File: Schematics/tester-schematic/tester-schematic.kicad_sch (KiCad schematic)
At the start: 1 part

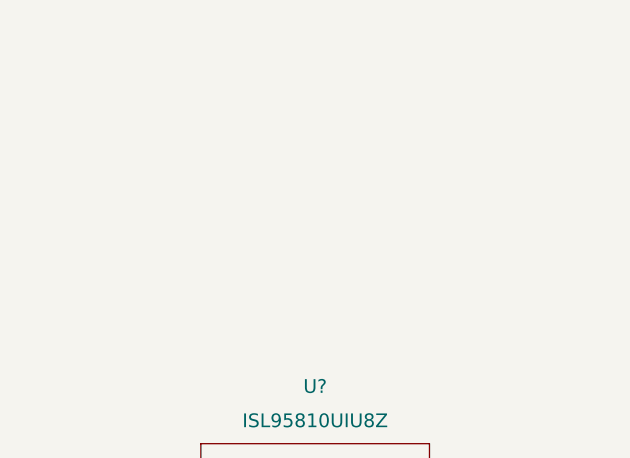
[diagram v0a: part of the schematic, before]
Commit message: added buck converter library
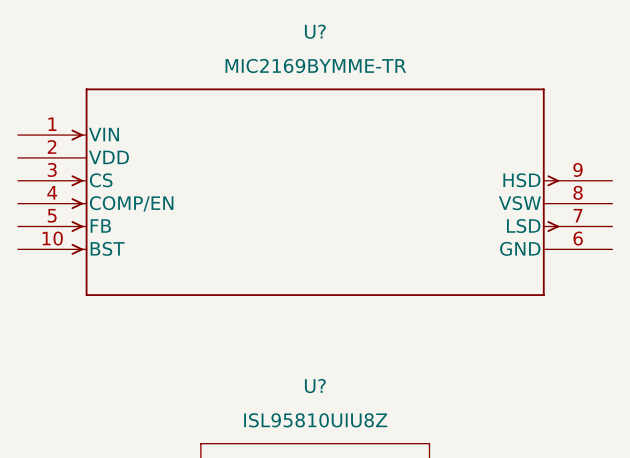
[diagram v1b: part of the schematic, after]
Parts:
- added U?: MIC2169BYMME-TR, MSOP-10_MM_MCH, symbol buck:MIC2169BYMME-TR
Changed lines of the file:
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@@
     (pin "8")
+  )
+  (symbol (lib_id "buck:MIC2169BYMME-TR") (at 104.14 52.07 0) (unit 1)
+    (in_bom yes) (on_board yes) (fields_autoplaced)
+    (property "Reference" "U?" (id 0) (at 137.16 40.64 0)
+      (effects (font (size 1.524 1.524)))
+    )
+    (property "Value" "MIC2169BYMME-TR" (id 1) (at 137.16 44.45 0)
+      (effects (font (size 1.524 1.524)))
+    )
+    (property "Footprint" "MSOP-10_MM_MCH" (id 2) (at 137.16 45.974 0)
+      (effects (font (size 1.524 1.524)) hide)
+    )
+    (property "Datasheet" "" (id 3) (at 104.14 52.07 0)
+      (effects (font (size 1.524 1.524)))
+    )
+    (pin "1")
+    (pin "10")
+    (pin "2")
+    (pin "3")
+    (pin "4")
+    (pin "5")
+    (pin "6")
+    (pin "7")
+    (pin "8")
+    (pin "9")
   )
   (sheet_instances
@@
       (reference "U?") (unit 1) (value "ISL95810UIU8Z") (footprint "MSOP8_3P05X3P05_INR")
     )
+    (path "/eba1abb3-bc61-46a2-bdc4-c956629aef7c"
+      (reference "U?") (unit 1) (value "MIC2169BYMME-TR") (footprint "MSOP-10_MM_MCH")
+    )
   )

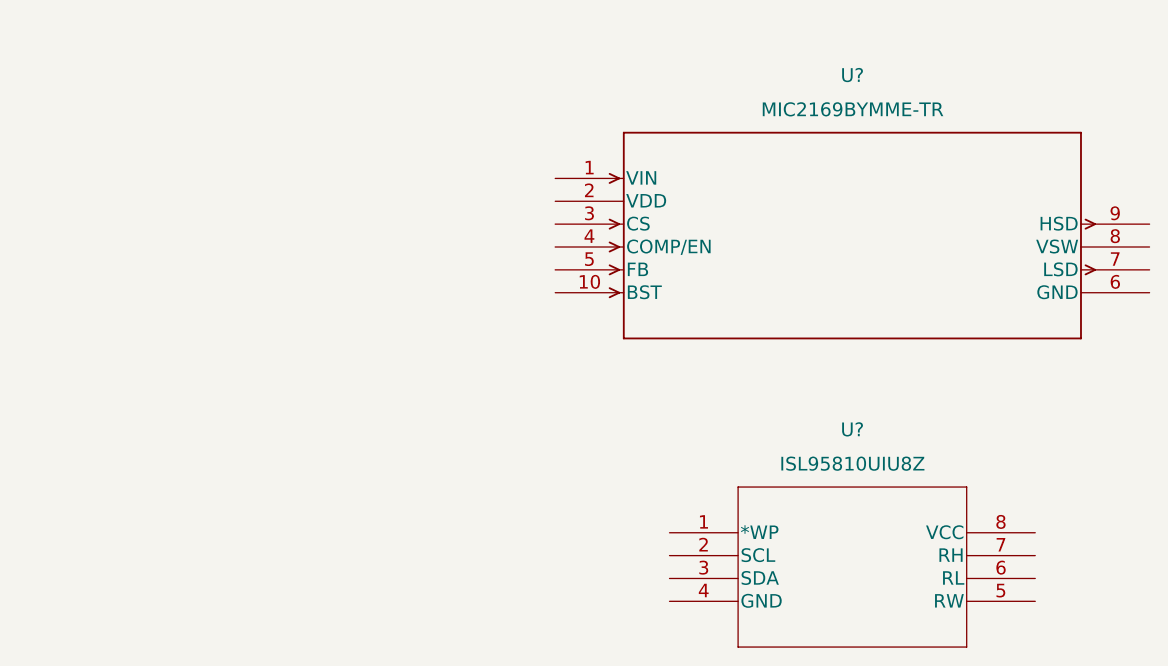
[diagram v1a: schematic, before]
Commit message: buck converter, dig pot, and surrounding components incomplete
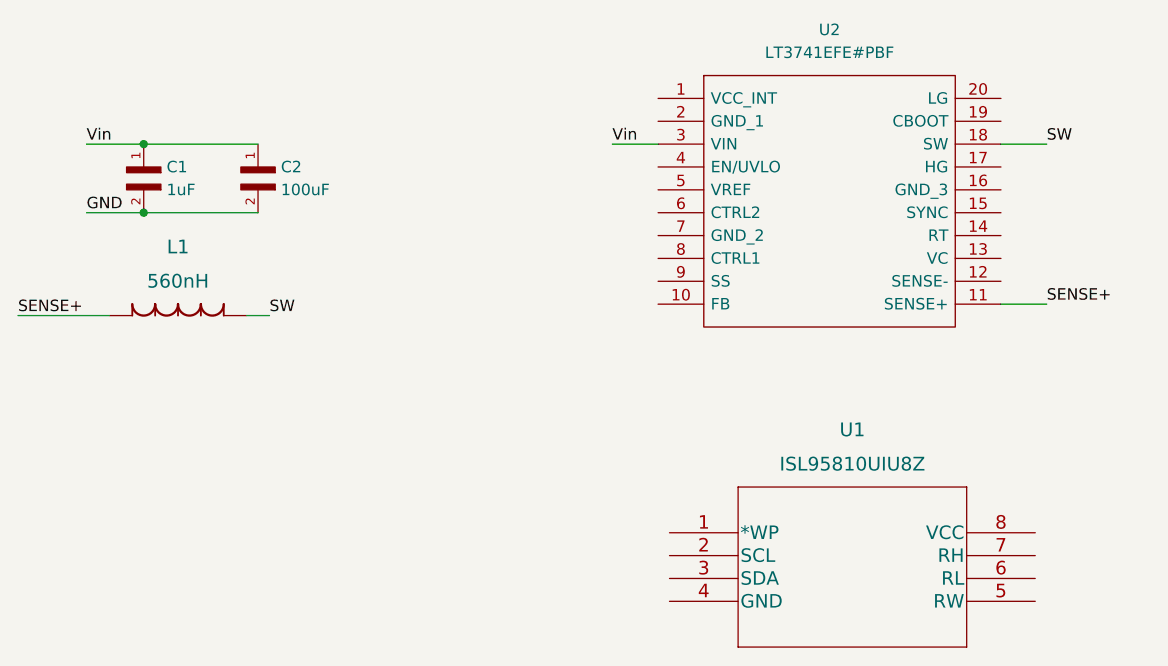
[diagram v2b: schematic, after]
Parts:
- removed U?: MIC2169BYMME-TR, MSOP-10_MM_MCH, symbol buck:MIC2169BYMME-TR
- added C1: 1uF, CAPC2012X127N, symbol 0805cap:S-0805
- added C2: 100uF, CAPC2012X127N, symbol 0805cap:S-0805
- added L1: 560nH, IND_IHLP-6767GZ_VIS, symbol 560nH_IND:IHLP6767GZERR56M01
- added U2: LT3741EFE#PBF, SOP65P640X120-20N, symbol Buck2:LT3741EFE#PBF
- gave numbers to parts that had none: 1
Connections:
- new net GND: C1.2, C2.2
- new net SENSE+: L1.2, U2.11 (SENSE+)
- new net SW: L1.1, U2.18 (SW)
- new net Vin: C1.1, C2.1, U2.3 (VIN)
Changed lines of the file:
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@@
 (kicad_sch (version 20211123) (generator eeschema)
   (paper "A4")
+  (junction (at 58.42 48.26) (diameter 0) (color 0 0 0 0)
+  )
+  (junction (at 58.42 55.88) (diameter 0) (color 0 0 0 0)
+  )
+  (wire (pts (xy 153.67 66.04) (xy 158.75 66.04))
+    (stroke (width 0) (type default) (color 0 0 0 0))
+  )
+  (wire (pts (xy 52.07 55.88) (xy 58.42 55.88))
+    (stroke (width 0) (type default) (color 0 0 0 0))
+  )
+  (wire (pts (xy 58.42 48.26) (xy 71.12 48.26))
+    (stroke (width 0) (type default) (color 0 0 0 0))
+  )
+  (wire (pts (xy 52.07 48.26) (xy 58.42 48.26))
+    (stroke (width 0) (type default) (color 0 0 0 0))
+  )
+  (wire (pts (xy 110.49 48.26) (xy 115.57 48.26))
+    (stroke (width 0) (type default) (color 0 0 0 0))
+  )
+  (wire (pts (xy 153.67 48.26) (xy 158.75 48.26))
+    (stroke (width 0) (type default) (color 0 0 0 0))
+  )
+  (wire (pts (xy 69.85 67.31) (xy 72.39 67.31))
+    (stroke (width 0) (type default) (color 0 0 0 0))
+  )
+  (wire (pts (xy 44.45 67.31) (xy 54.61 67.31))
+    (stroke (width 0) (type default) (color 0 0 0 0))
+  )
+  (wire (pts (xy 58.42 55.88) (xy 71.12 55.88))
+    (stroke (width 0) (type default) (color 0 0 0 0))
+  )
+  (label "SW" (at 158.75 48.26 0)
+    (effects (font (size 1.27 1.27)) (justify left bottom))
+  )
+  (label "SENSE+" (at 158.75 66.04 0)
+    (effects (font (size 1.27 1.27)) (justify left bottom))
+  )
+  (label "GND" (at 52.07 55.88 0)
+    (effects (font (size 1.27 1.27)) (justify left bottom))
+  )
+  (label "SW" (at 72.39 67.31 0)
+    (effects (font (size 1.27 1.27)) (justify left bottom))
+  )
+  (label "Vin" (at 110.49 48.26 0)
+    (effects (font (size 1.27 1.27)) (justify left bottom))
+  )
+  (label "SENSE+" (at 44.45 67.31 0)
+    (effects (font (size 1.27 1.27)) (justify left bottom))
+  )
+  (label "Vin" (at 52.07 48.26 0)
+    (effects (font (size 1.27 1.27)) (justify left bottom))
+  )
+  (symbol (lib_id "0805cap:S-0805") (at 71.12 53.34 90) (unit 1)
+    (in_bom yes) (on_board yes) (fields_autoplaced)
+    (property "Reference" "C2" (id 0) (at 73.66 50.7999 90)
+      (effects (font (size 1.27 1.27)) (justify right))
+    )
+    (property "Value" "100uF" (id 1) (at 73.66 53.3399 90)
+      (effects (font (size 1.27 1.27)) (justify right))
+    )
+    (property "Footprint" "CAPC2012X127N" (id 2) (at 71.12 53.34 0)
+      (effects (font (size 1.27 1.27)) (justify left bottom) hide)
+    )
+    (property "Datasheet" "" (id 3) (at 71.12 53.34 0)
+      (effects (font (size 1.27 1.27)) (justify left bottom) hide)
+    )
+    (pin "1")
+    (pin "2")
+  )
+  (symbol (lib_id "0805cap:S-0805") (at 58.42 53.34 90) (unit 1)
+    (in_bom yes) (on_board yes) (fields_autoplaced)
+    (property "Reference" "C1" (id 0) (at 60.96 50.7999 90)
+      (effects (font (size 1.27 1.27)) (justify right))
+    )
+    (property "Value" "1uF" (id 1) (at 60.96 53.3399 90)
+      (effects (font (size 1.27 1.27)) (justify right))
+    )
+    (property "Footprint" "CAPC2012X127N" (id 2) (at 58.42 53.34 0)
+      (effects (font (size 1.27 1.27)) (justify left bottom) hide)
+    )
+    (property "Datasheet" "" (id 3) (at 58.42 53.34 0)
+      (effects (font (size 1.27 1.27)) (justify left bottom) hide)
+    )
+    (pin "1")
+    (pin "2")
+  )
   (symbol (lib_id "digipot:ISL95810UIU8Z") (at 116.84 91.44 0) (unit 1)
     (in_bom yes) (on_board yes) (fields_autoplaced)
-    (property "Reference" "U?" (id 0) (at 137.16 80.01 0)
+    (property "Reference" "U1" (id 0) (at 137.16 80.01 0)
       (effects (font (size 1.524 1.524)))
     )
@@
     (pin "8")
   )
-  (symbol (lib_id "buck:MIC2169BYMME-TR") (at 104.14 52.07 0) (unit 1)
-    (in_bom yes) (on_board yes) (fields_autoplaced)
-    (property "Reference" "U?" (id 0) (at 137.16 40.64 0)
-      (effects (font (size 1.524 1.524)))
-    )
-    (property "Value" "MIC2169BYMME-TR" (id 1) (at 137.16 44.45 0)
-      (effects (font (size 1.524 1.524)))
-    )
-    (property "Footprint" "MSOP-10_MM_MCH" (id 2) (at 137.16 45.974 0)
-      (effects (font (size 1.524 1.524)) hide)
-    )
-    (property "Datasheet" "" (id 3) (at 104.14 52.07 0)
-      (effects (font (size 1.524 1.524)))
+  (symbol (lib_id "Buck2:LT3741EFE#PBF") (at 115.57 43.18 0) (unit 1)
+    (in_bom yes) (on_board yes) (fields_autoplaced)
+    (property "Reference" "U2" (id 0) (at 134.62 35.56 0))
+    (property "Value" "LT3741EFE#PBF" (id 1) (at 134.62 38.1 0))
+    (property "Footprint" "SOP65P640X120-20N" (id 2) (at 149.86 40.64 0)
+      (effects (font (size 1.27 1.27)) (justify left) hide)
+    )
+    (property "Datasheet" "https://www.analog.com/media/en/technical-documentation/data-sheets/37411fg.pdf" (id 3) (at 149.86 43.18 0)
+      (effects (font (size 1.27 1.27)) (justify left) hide)
+    )
+    (property "Description" "Linear Technology, LT3741EFE#PBF Step-Down Switching Regulator 20A, 0  34 V, 20-Pin TSSOP" (id 4) (at 149.86 45.72 0)
+      (effects (font (size 1.27 1.27)) (justify left) hide)
+    )
+    (property "Height" "1.2" (id 5) (at 149.86 48.26 0)
+      (effects (font (size 1.27 1.27)) (justify left) hide)
+    )
+    (property "Manufacturer_Name" "Analog Devices" (id 6) (at 149.86 50.8 0)
+      (effects (font (size 1.27 1.27)) (justify left) hide)
+    )
+    (property "Manufacturer_Part_Number" "LT3741EFE#PBF" (id 7) (at 149.86 53.34 0)
+      (effects (font (size 1.27 1.27)) (justify left) hide)
+    )
+    (property "Mouser Part Number" "584-LT3741EFE#PBF" (id 8) (at 149.86 55.88 0)
+      (effects (font (size 1.27 1.27)) (justify left) hide)
+    )
+    (property "Mouser Price/Stock" "https://www.mouser.co.uk/ProductDetail/Analog-Devices-Linear-Technology/LT3741EFEPBF?qs=hVkxg5c3xu9OVpTbq3Fh0A%3D%3D" (id 9) (at 149.86 58.42 0)
+      (effects (font (size 1.27 1.27)) (justify left) hide)
+    )
+    (property "Arrow Part Number" "LT3741EFE#PBF" (id 10) (at 149.86 60.96 0)
+      (effects (font (size 1.27 1.27)) (justify left) hide)
+    )
+    (property "Arrow Price/Stock" "https://www.arrow.com/en/products/lt3741efepbf/linear-technology" (id 11) (at 149.86 63.5 0)
+      (effects (font (size 1.27 1.27)) (justify left) hide)
     )
     (pin "1")
     (pin "10")
-    (pin "2")
+    (pin "11")
+    (pin "12")
+    (pin "13")
+    (pin "14")
+    (pin "15")
+    (pin "16")
+    (pin "17")
+    (pin "18")
+    (pin "19")
+    (pin "2")
+    (pin "20")
     (pin "3")
     (pin "4")
@@
     (pin "9")
   )
+  (symbol (lib_id "560nH_IND:IHLP6767GZERR56M01") (at 54.61 67.31 0) (unit 1)
+    (in_bom yes) (on_board yes) (fields_autoplaced)
+    (property "Reference" "L1" (id 0) (at 62.23 59.69 0)
+      (effects (font (size 1.524 1.524)))
+    )
+    (property "Value" "560nH" (id 1) (at 62.23 63.5 0)
+      (effects (font (size 1.524 1.524)))
+    )
+    (property "Footprint" "IND_IHLP-6767GZ_VIS" (id 2) (at 61.595 74.549 0)
+      (effects (font (size 1.524 1.524)) hide)
+    )
+    (property "Datasheet" "" (id 3) (at 54.61 67.31 0)
+      (effects (font (size 1.524 1.524)))
+    )
+    (pin "1")
+    (pin "2")
+  )
   (sheet_instances
     (path "/" (page "1"))
   )
   (symbol_instances
+    (path "/b6f3c762-1917-4cf7-971d-748bdf1de22f"
+      (reference "C1") (unit 1) (value "1uF") (footprint "CAPC2012X127N")
+    )
+    (path "/02c15933-45ef-433e-94b4-9c47740182e8"
+      (reference "C2") (unit 1) (value "100uF") (footprint "CAPC2012X127N")
+    )
+    (path "/f3f29d99-7ed9-4a06-bdd2-c55fa719f787"
+      (reference "L1") (unit 1) (value "560nH") (footprint "IND_IHLP-6767GZ_VIS")
+    )
     (path "/c7e9425a-7abd-432d-b431-d0efb89a2f68"
-      (reference "U?") (unit 1) (value "ISL95810UIU8Z") (footprint "MSOP8_3P05X3P05_INR")
-    )
-    (path "/eba1abb3-bc61-46a2-bdc4-c956629aef7c"
-      (reference "U?") (unit 1) (value "MIC2169BYMME-TR") (footprint "MSOP-10_MM_MCH")
-    )
-  )
+      (reference "U1") (unit 1) (value "ISL95810UIU8Z") (footprint "MSOP8_3P05X3P05_INR")
+    )
+    (path "/cf2a5d5d-b207-4509-8e31-e34e73696326"
+      (reference "U2") (unit 1) (value "LT3741EFE#PBF") (footprint "SOP65P640X120-20N")
+    )
+  )
